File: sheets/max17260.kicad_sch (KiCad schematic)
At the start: 4 parts, among them U6 MAX17260

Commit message: Changes to fuel gauge and charger sheets
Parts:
- renumbered C22 to C?, C23 to C?, R21 to R?, U6 to U?
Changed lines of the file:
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@@
 		(on_board yes)
 		(dnp no)
-		(property "Reference" "C22"
+		(property "Reference" "C?"
 			(at 71.882 64.77 0)
 			(effects
@@
 		)
 		(instances
+			(project "powerups"
+				(path "/351775ff-22dd-4601-a146-0ae5bb7b1807/79a6a83b-266a-4a69-901f-f515d0156029"
+					(reference "C?")
+					(unit 1)
+				)
+			)
 			(project "esp32s3-powerfeather"
 				(path "/5be6a852-fa78-49fa-bb8c-8d5ad39f4b26/a940761a-0d45-4491-ba89-ec093a8f239f/b14ae25c-1044-42b2-88e6-486f3cf2e161"
@@
 		(on_board yes)
 		(dnp no)
-		(property "Reference" "C23"
+		(property "Reference" "C?"
 			(at 126.746 75.692 0)
 			(effects
@@
 		)
 		(instances
+			(project "powerups"
+				(path "/351775ff-22dd-4601-a146-0ae5bb7b1807/79a6a83b-266a-4a69-901f-f515d0156029"
+					(reference "C?")
+					(unit 1)
+				)
+			)
 			(project "esp32s3-powerfeather"
 				(path "/5be6a852-fa78-49fa-bb8c-8d5ad39f4b26/a940761a-0d45-4491-ba89-ec093a8f239f/b14ae25c-1044-42b2-88e6-486f3cf2e161"
@@
 		(on_board yes)
 		(dnp no)
-		(property "Reference" "R21"
+		(property "Reference" "R?"
 			(at 133.096 60.96 0)
 			(effects
@@
 		)
 		(instances
+			(project "powerups"
+				(path "/351775ff-22dd-4601-a146-0ae5bb7b1807/79a6a83b-266a-4a69-901f-f515d0156029"
+					(reference "R?")
+					(unit 1)
+				)
+			)
 			(project "esp32s3-powerfeather"
 				(path "/5be6a852-fa78-49fa-bb8c-8d5ad39f4b26/a940761a-0d45-4491-ba89-ec093a8f239f/b14ae25c-1044-42b2-88e6-486f3cf2e161"
@@
 		(dnp no)
 		(fields_autoplaced yes)
-		(property "Reference" "U6"
+		(property "Reference" "U?"
 			(at 105.41 78.74 0)
 			(effects
@@
 		)
 		(instances
+			(project "powerups"
+				(path "/351775ff-22dd-4601-a146-0ae5bb7b1807/79a6a83b-266a-4a69-901f-f515d0156029"
+					(reference "U?")
+					(unit 1)
+				)
+			)
 			(project "esp32s3-powerfeather"
 				(path "/5be6a852-fa78-49fa-bb8c-8d5ad39f4b26/a940761a-0d45-4491-ba89-ec093a8f239f/b14ae25c-1044-42b2-88e6-486f3cf2e161"

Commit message: Run designator annotations
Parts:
- gave numbers to parts that had none: 4
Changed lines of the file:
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@@
 		(on_board yes)
 		(dnp no)
-		(property "Reference" "C?"
+		(property "Reference" "C14"
 			(at 71.882 64.77 0)
 			(effects
@@
 			(project "powerups"
 				(path "/351775ff-22dd-4601-a146-0ae5bb7b1807/79a6a83b-266a-4a69-901f-f515d0156029"
-					(reference "C?")
+					(reference "C14")
 					(unit 1)
 				)
@@
 		(on_board yes)
 		(dnp no)
-		(property "Reference" "C?"
+		(property "Reference" "C15"
 			(at 126.746 75.692 0)
 			(effects
@@
 			(project "powerups"
 				(path "/351775ff-22dd-4601-a146-0ae5bb7b1807/79a6a83b-266a-4a69-901f-f515d0156029"
-					(reference "C?")
+					(reference "C15")
 					(unit 1)
 				)
@@
 		(on_board yes)
 		(dnp no)
-		(property "Reference" "R?"
+		(property "Reference" "R24"
 			(at 133.096 60.96 0)
 			(effects
@@
 			(project "powerups"
 				(path "/351775ff-22dd-4601-a146-0ae5bb7b1807/79a6a83b-266a-4a69-901f-f515d0156029"
-					(reference "R?")
+					(reference "R24")
 					(unit 1)
 				)
@@
 		(dnp no)
 		(fields_autoplaced yes)
-		(property "Reference" "U?"
+		(property "Reference" "U7"
 			(at 105.41 78.74 0)
 			(effects
@@
 			(project "powerups"
 				(path "/351775ff-22dd-4601-a146-0ae5bb7b1807/79a6a83b-266a-4a69-901f-f515d0156029"
-					(reference "U?")
-					(unit 1)
-				)
+					(reference "U7")
+					(unit 1)
+				)

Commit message: Renumber components for powerups
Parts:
- renumbered C14 to C19, C15 to C20, R24 to R30
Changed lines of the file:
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@@
 		(on_board yes)
 		(dnp no)
-		(property "Reference" "C14"
+		(property "Reference" "C19"
 			(at 71.882 64.77 0)
 			(effects
@@
 			(project "powerups"
 				(path "/351775ff-22dd-4601-a146-0ae5bb7b1807/79a6a83b-266a-4a69-901f-f515d0156029"
-					(reference "C14")
+					(reference "C19")
 					(unit 1)
 				)
@@
 		(on_board yes)
 		(dnp no)
-		(property "Reference" "C15"
+		(property "Reference" "C20"
 			(at 126.746 75.692 0)
 			(effects
@@
 			(project "powerups"
 				(path "/351775ff-22dd-4601-a146-0ae5bb7b1807/79a6a83b-266a-4a69-901f-f515d0156029"
-					(reference "C15")
+					(reference "C20")
 					(unit 1)
 				)
@@
 		(on_board yes)
 		(dnp no)
-		(property "Reference" "R24"
+		(property "Reference" "R30"
 			(at 133.096 60.96 0)
 			(effects
@@
 			(project "powerups"
 				(path "/351775ff-22dd-4601-a146-0ae5bb7b1807/79a6a83b-266a-4a69-901f-f515d0156029"
-					(reference "R24")
-					(unit 1)
-				)
+					(reference "R30")
+					(unit 1)
+				)

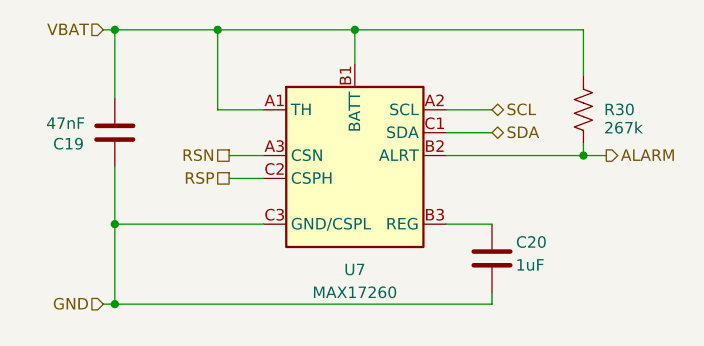
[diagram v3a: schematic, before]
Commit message: Fix max17260 circuit
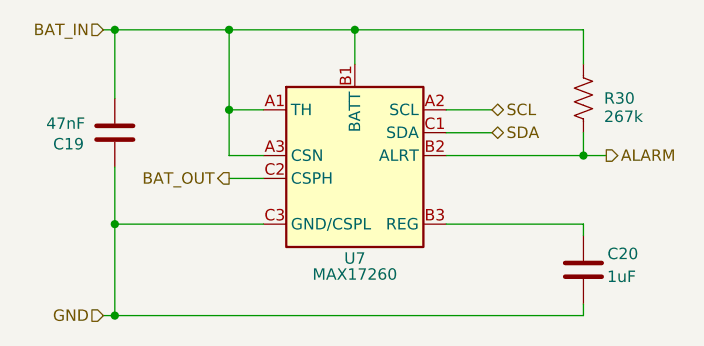
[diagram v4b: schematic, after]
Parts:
- R30: MPN 603-AC0402FR-07267KL -> (none); Mouser (none) -> 603-AC0402FR-07267KL
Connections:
- net VBAT is gone; now on net BAT_IN: C19.1, R30.1, U7.A1 (TH), U7.B1 (BATT)
- net RSN renamed BAT_IN
- net RSP renamed BAT_OUT
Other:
- company: (none) -> PowerFeather
- title: (none) -> MAX17260 fuel guage circuit
- moved on the sheet: C20, R30
